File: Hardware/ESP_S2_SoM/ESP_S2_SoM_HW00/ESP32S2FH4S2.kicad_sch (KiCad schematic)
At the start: 31 parts, among them SW401 SW_Push, SW402 SW_Push, U401 ESP32-S2FH4, Y601 Crystal_GND24_Small

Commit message: Working on routing
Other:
- title: PSoM - ESP S2 -> PSoM - ESP32 S2
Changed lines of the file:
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@@
   (paper "A4")
   (title_block
-    (title "PSoM - ESP S2")
+    (title "PSoM - ESP32 S2")
     (date "2023-04-17")
     (rev "HW00")

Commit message: Routing is done
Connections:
- net ANT: now reaches ANT401.1 (A), C406.1, L401.1
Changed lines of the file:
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@@
+    (effects (font (size 1.27 1.27)) (justify right bottom))
+  )
+  (label "ANT" (at 170.18 83.82 180) (fields_autoplaced)
     (effects (font (size 1.27 1.27)) (justify right bottom))
   )

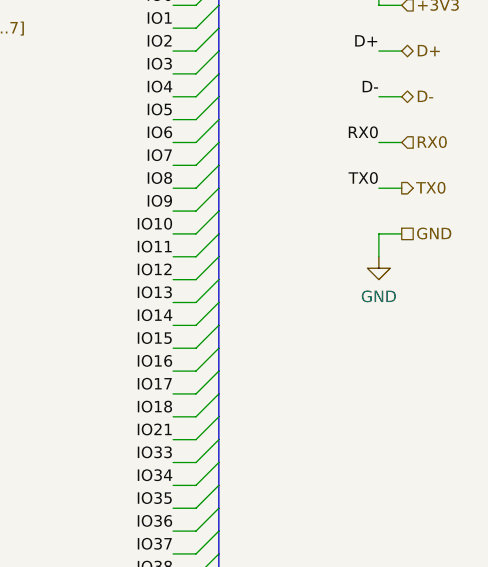
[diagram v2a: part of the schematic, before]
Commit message: quick pinout adjustement
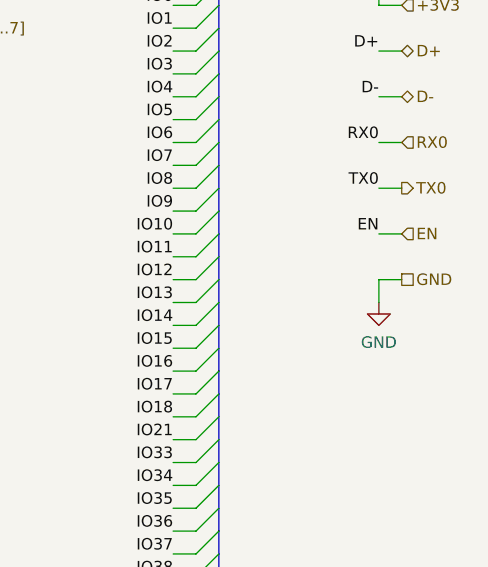
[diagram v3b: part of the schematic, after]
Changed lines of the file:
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@@
+    (stroke (width 0) (type default))
+  )
+  (wire (pts (xy 264.16 48.26) (xy 266.7 48.26))
     (stroke (width 0) (type default))
   )
@@
     (stroke (width 0) (type default))
   )
-  (wire (pts (xy 264.16 48.26) (xy 266.7 48.26))
+  (wire (pts (xy 264.16 53.34) (xy 266.7 53.34))
     (stroke (width 0) (type default))
   )
@@
     (stroke (width 0) (type default))
   )
-  (wire (pts (xy 264.16 50.8) (xy 264.16 48.26))
+  (wire (pts (xy 264.16 55.88) (xy 264.16 53.34))
     (stroke (width 0) (type default))
   )
@@
     (effects (font (size 1.27 1.27)) (justify right bottom))
   )
+  (label "EN" (at 264.16 48.26 180) (fields_autoplaced)
+    (effects (font (size 1.27 1.27)) (justify right bottom))
+  )
   (label "IO42" (at 241.3 96.52 180) (fields_autoplaced)
     (effects (font (size 1.27 1.27)) (justify right bottom))
@@
     (effects (font (size 1.27 1.27)) (justify left))
   )
-  (hierarchical_label "GND" (shape passive) (at 266.7 48.26 0) (fields_autoplaced)
+  (hierarchical_label "GND" (shape passive) (at 266.7 53.34 0) (fields_autoplaced)
     (effects (font (size 1.27 1.27)) (justify left))
   )
   (hierarchical_label "D-" (shape bidirectional) (at 266.7 33.02 0) (fields_autoplaced)
+    (effects (font (size 1.27 1.27)) (justify left))
+  )
+  (hierarchical_label "EN" (shape input) (at 266.7 48.26 0) (fields_autoplaced)
     (effects (font (size 1.27 1.27)) (justify left))
   )
@@
     )
   )
-  (symbol (lib_id "power:GND") (at 264.16 50.8 0) (unit 1)
-    (in_bom yes) (on_board yes) (dnp no) (fields_autoplaced)
-    (property "Reference" "#PWR0403" (at 264.16 57.15 0)
-      (effects (font (size 1.27 1.27)) hide)
-    )
-    (property "Value" "GND" (at 264.16 55.2434 0)
-      (effects (font (size 1.27 1.27)))
-    )
-    (property "Footprint" "" (at 264.16 50.8 0)
-      (effects (font (size 1.27 1.27)) hide)
-    )
-    (property "Datasheet" "" (at 264.16 50.8 0)
-      (effects (font (size 1.27 1.27)) hide)
-    )
+  (symbol (lib_id "power:GND") (at 264.16 55.88 0) (unit 1)
+    (in_bom yes) (on_board yes) (dnp no) (fields_autoplaced)
+    (property "Reference" "#PWR0403" (at 264.16 62.23 0)
+      (effects (font (size 1.27 1.27)) hide)
+    )
+    (property "Value" "GND" (at 264.16 60.3234 0)
+      (effects (font (size 1.27 1.27)))
+    )
+    (property "Footprint" "" (at 264.16 55.88 0)
+      (effects (font (size 1.27 1.27)) hide)
+    )
+    (property "Datasheet" "" (at 264.16 55.88 0)
+      (effects (font (size 1.27 1.27)) hide)
+    )

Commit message: Small cartouche mistake
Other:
- title: PSoM - ESP32 S2 -> PSoM - ESP S2
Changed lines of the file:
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@@
   (paper "A4")
   (title_block
-    (title "PSoM - ESP32 S2")
+    (title "PSoM - ESP S2")
     (date "2023-04-17")
     (rev "HW00")
